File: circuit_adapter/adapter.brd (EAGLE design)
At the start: 39.6 x 34.3 mm, 12 parts, among them CN1 5035521020, CN3 5035521020, X1 2510-

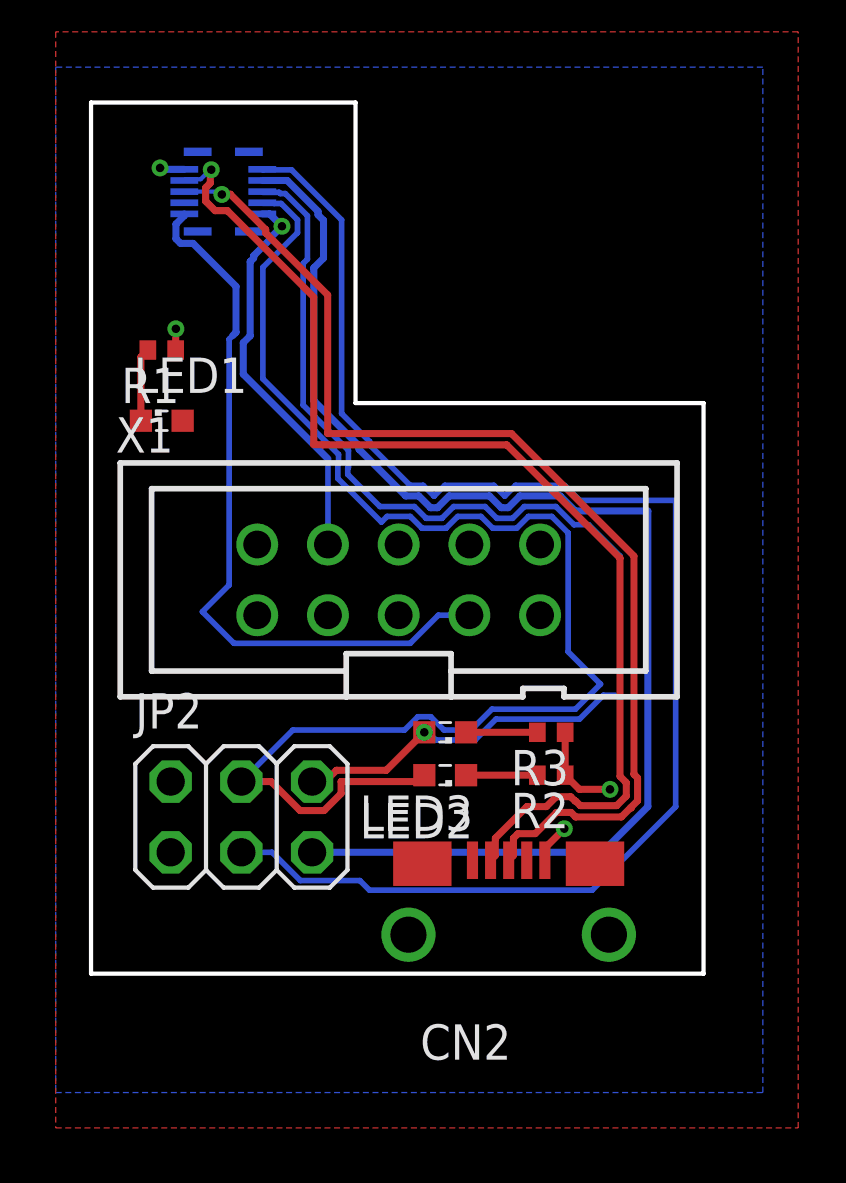
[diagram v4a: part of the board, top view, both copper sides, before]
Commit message: Modified adapter circuit
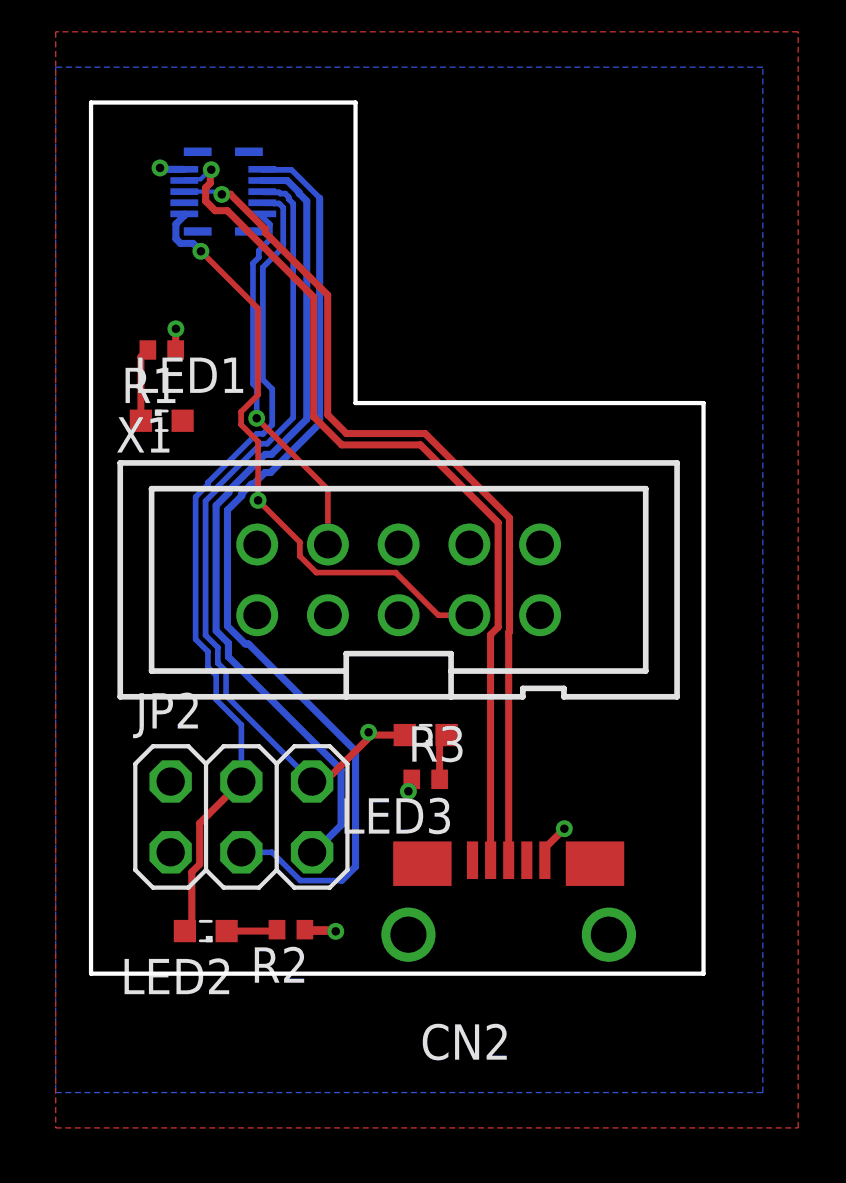
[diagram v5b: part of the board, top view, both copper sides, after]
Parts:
- moved R2 10.9 mm to (7.18, 4.58)
- moved LED2 10.3 mm to (4.12, 4.53)
- moved R3 4.82 mm to (12.0, 9.98), turned to 0 degrees
- moved LED3 0.71 mm to (12.0, 11.6)
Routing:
- net GPIO0: track 50.9 -> 30.1 mm
- net TX1: track 53.0 -> 34.7 mm
- net RX1: track 47.3 -> 29.2 mm
- net GPIO1: track 41.3 -> 29.1 mm
- net D-: track 42.8 -> 34.0 mm
- net D+: track 39.4 -> 31.4 mm
- net C2CK: track 26.5 -> 22.0 mm, vias 0 -> 2
- net N$3: track 2.56 -> 1.69 mm
- net GND: track 5.55 -> 4.73 mm, vias 3 -> 4
- net C2D: track 14.2 -> 13.4 mm
- net N$2: track 2.56 -> 1.83 mm

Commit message: Modified adapter circuit and added garber zip
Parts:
- removed CN3: 5035521020, connector:5035521020
- removed CN4: (no value), connector:USB
- moved LED3 9.61 mm to (2.43, 11.0), turned to 0 degrees
- moved R3 9.54 mm to (2.53, 9.02), turned to 180 degrees
- moved R2 4.67 mm to (2.53, 4.98)
- moved LED2 2.98 mm to (2.48, 7.02), turned to 0 degrees
- moved JP2 1.74 mm to (7.02, 8.00), turned to 90 degrees
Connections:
- removed net D+2: CN3.5, CN4.D+
- removed net D-2: CN3.3, CN4.D-
- removed net GND2: CN3.7, CN4.GND
- removed net VBUS2: CN3.1, CN4.VBUS
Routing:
- net VBUS2: track 8.98 -> 0.00 mm, vias 1 -> 0
- net D-2: track 7.83 -> 0.00 mm, vias 1 -> 0
- net TX1: track 34.7 -> 29.2 mm
- net GND: track 4.73 -> 9.80 mm, vias 4 -> 2
- net RX1: track 29.2 -> 25.2 mm
- net GND2: track 3.29 -> 0.00 mm, vias 1 -> 0
- net GPIO1: track 29.1 -> 26.3 mm, vias 1 -> 0
- net D+2: track 2.08 -> 0.00 mm, vias 1 -> 0
- net GPIO0: track 30.1 -> 28.8 mm
- net C2CK: vias 2 -> 1
- removed copper zone on layer 16, net GND2
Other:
- board size 39.6 x 34.3 mm -> 22 x 31.3 mm

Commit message: Modified parts values
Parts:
- R2: value 5.1 -> 5.1k
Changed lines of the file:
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@@
 <attribute name="VALUE" x="3.175" y="27.305" size="1.27" layer="27" rot="R180"/>
 </element>
-<element name="R2" library="rcl" library_urn="urn:adsk.eagle:library:334" package="R0402" package3d_urn="urn:adsk.eagle:package:23547/2" value="5.1" x="2.53" y="4.98" rot="R180">
+<element name="R2" library="rcl" library_urn="urn:adsk.eagle:library:334" package="R0402" package3d_urn="urn:adsk.eagle:package:23547/2" value="5.1k" x="2.53" y="4.98" rot="R180">
 <attribute name="SPICEPREFIX" value="R" x="2.53" y="4.98" size="1.778" layer="27" rot="R180" display="off"/>
 <attribute name="VALUE" x="3.165" y="6.885" size="1.27" layer="27" rot="R180"/>

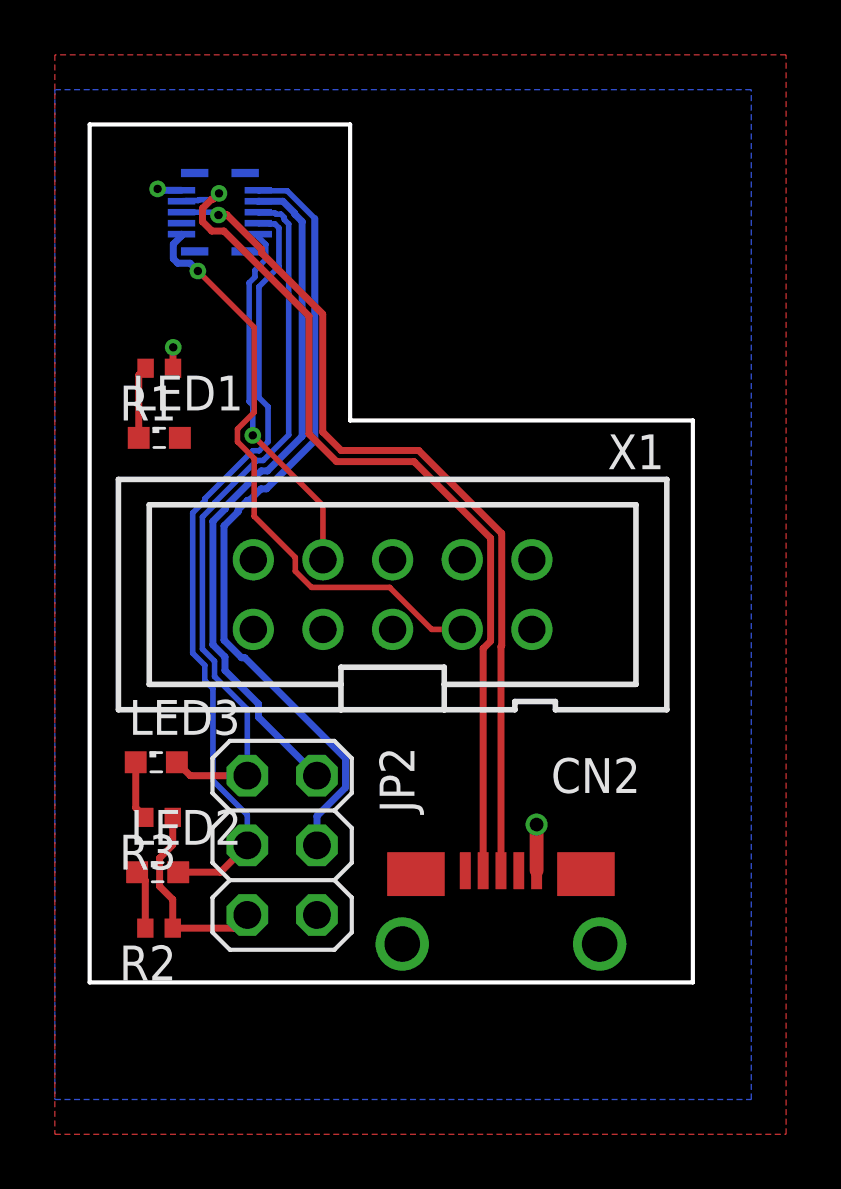
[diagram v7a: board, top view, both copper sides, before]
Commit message: Modified adapter circuit
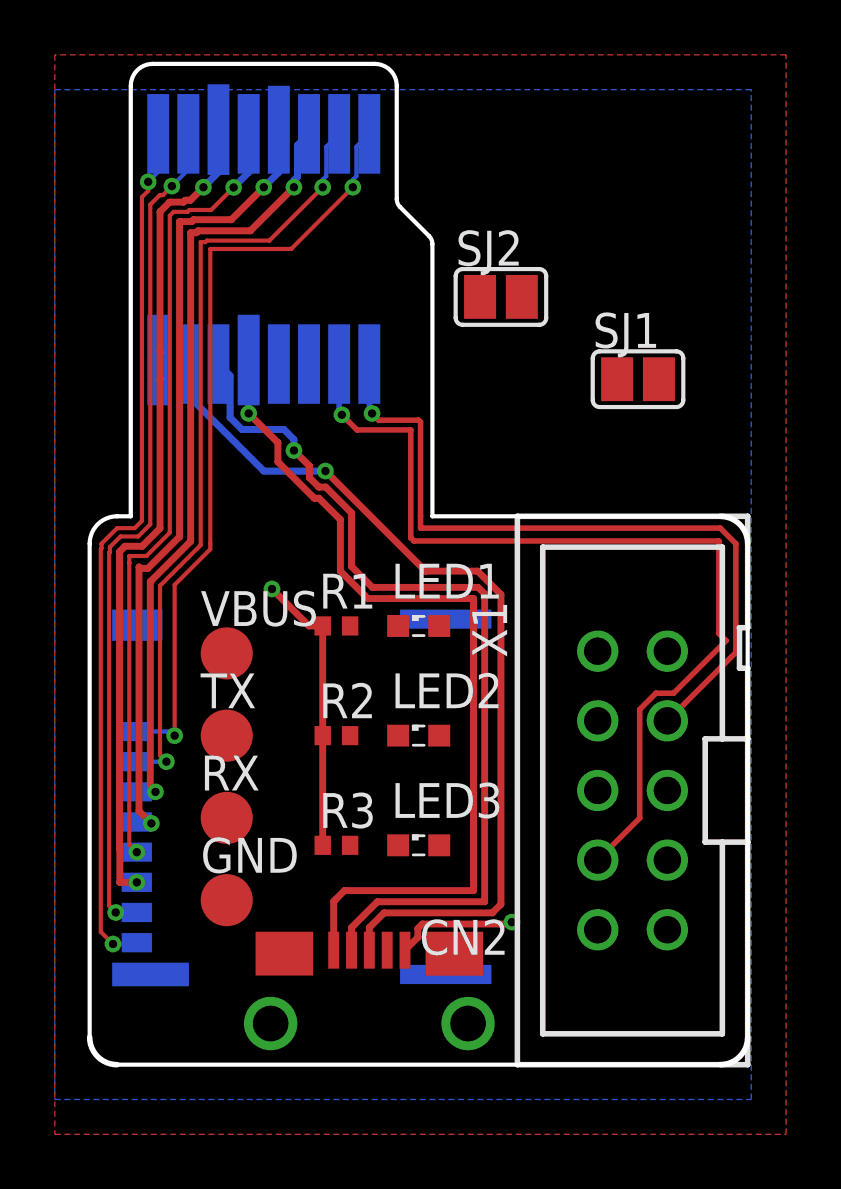
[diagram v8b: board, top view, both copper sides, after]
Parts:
- removed CN1: 5035521020, connector:5035521020
- removed JP2: (no value), pinhead:2X03
- added CN3: MICROSD_BARE, connector:MICROSD
- added CN4: VIRTUALGIMAL, connector:VIRTUALGIMBAL
- added CN5: MICROSD_WM11190CT-ND, connector:5033981892
- added GND, RX, TX, VBUS: PTR1TP19R, testpad:TP19R
- added SJ1, SJ2: (no value), jumper:SJ
- R1, R2, R3: value 5.1k -> 10k
- moved LED1 11.7 mm to (12.0, 16.0)
- moved R1 11.4 mm to (9.00, 16.0), turned to 0 degrees
- moved X1 11.3 mm to (19.8, 10.0), turned to 90 degrees
- moved LED2 10.7 mm to (12.0, 12.0)
- moved LED3 10.0 mm to (12.0, 8.00)
- moved R2 9.55 mm to (9.00, 12.0), turned to 0 degrees
- moved R3 6.55 mm to (9.00, 8.00), turned to 0 degrees
- moved CN2 5.61 mm to (10.2, 1.50)
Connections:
- removed net GND: CN1.7, CN2.5_GND, JP2.2, R1.1, R2.1, R3.1, X1.2, X1.3, X1.9
- removed net GPIO0: CN1.8, JP2.4, LED2.A
- removed net GPIO1: CN1.6, JP2.6, LED3.A
- new net DGND: CN2.5_GND, CN4.8, GND.TP, R1.1, R2.1, R3.1, X1.2, X1.3, X1.9
- new net N$10: CN3.7, CN5.DAT0
- new net N$11: CN3.8, CN5.DAT1
- new net N$12: LED2.A, SJ1.1
- new net N$13: LED3.A, SJ2.1
- new net N$4: CN3.1, CN5.DAT2
- new net N$5: CN3.2, CN5.CD/DAT3
- new net N$6: CN3.3, CN5.CMD
- new net N$7: CN3.4, CN5.VDD
- new net N$8: CN3.5, CN5.CLK
- new net N$9: CN3.6, CN5.VSS
- net C2CK: now also CN4.1; no longer CN1.9
- net C2D: now also CN4.2; no longer CN1.10
- net D+: now also CN4.7; no longer CN1.5
- net D-: now also CN4.6; no longer CN1.3
- net RX1: now also CN4.3, RX.TP, SJ2.2; no longer CN1.4, JP2.5
- net TX1: now also CN4.4, SJ1.2, TX.TP; no longer CN1.2, JP2.3
- net VBUS: now also CN4.5, VBUS.TP; no longer CN1.1, JP2.1
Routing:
- net N$11: track 0.00 -> 31.9 mm, vias 0 -> 2
- net VBUS: track 0.89 -> 32.2 mm
- net N$10: track 0.00 -> 30.9 mm, vias 0 -> 2
- net N$9: track 0.00 -> 30.3 mm, vias 0 -> 2
- net N$7: track 0.00 -> 29.5 mm, vias 0 -> 2
- net N$8: track 0.00 -> 29.2 mm, vias 0 -> 2
- net TX1: track 29.2 -> 0.00 mm
- net GPIO0: track 28.8 -> 0.00 mm
- net N$6: track 0.00 -> 28.4 mm, vias 0 -> 2
- net N$5: track 0.00 -> 28.2 mm, vias 0 -> 2
- net N$4: track 0.00 -> 28.1 mm, vias 0 -> 2
- net GPIO1: track 26.3 -> 0.00 mm
- net RX1: track 25.2 -> 0.00 mm
- net C2D: track 13.4 -> 33.9 mm
- net DGND: track 0.00 -> 14.9 mm, vias 0 -> 2
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- added copper zone on layer 16, net DGND
- removed copper zone on layer 16, net GND
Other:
- board size 22 x 31.3 mm -> 24 x 36.5 mm
